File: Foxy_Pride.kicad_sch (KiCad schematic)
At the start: 30 parts, among them U1 TLC555CDR, U2 74HC4017D

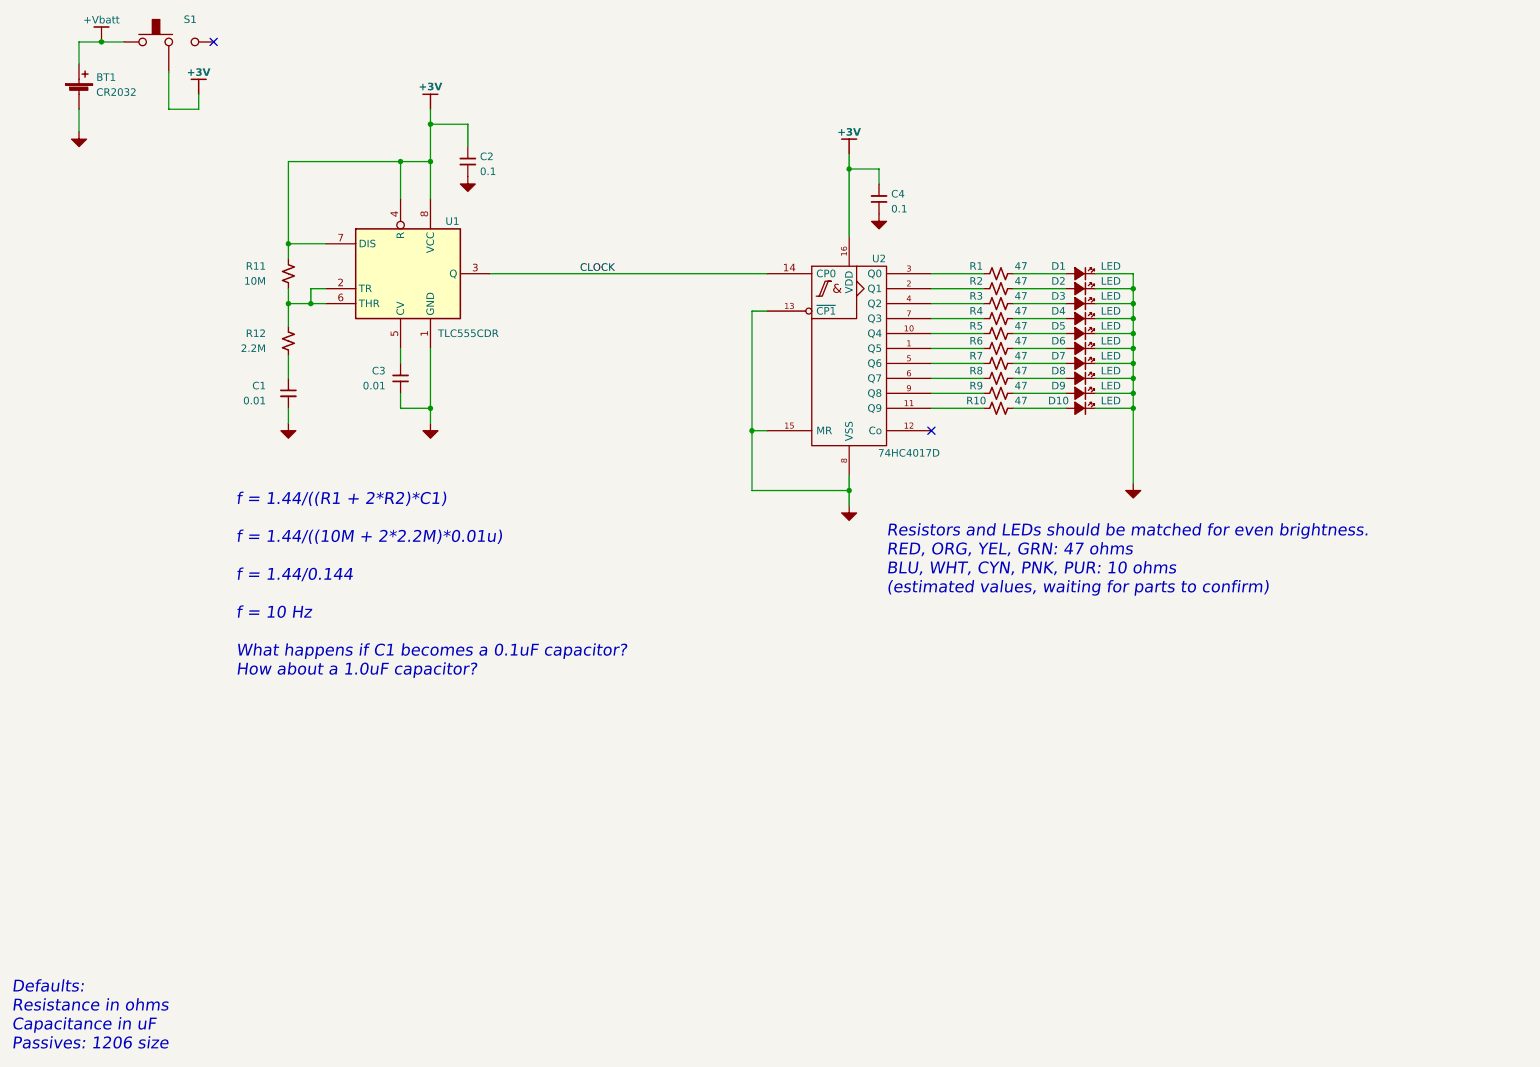
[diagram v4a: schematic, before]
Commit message: Changed schematic layout. Put resistor in correct spot. Update PCB.
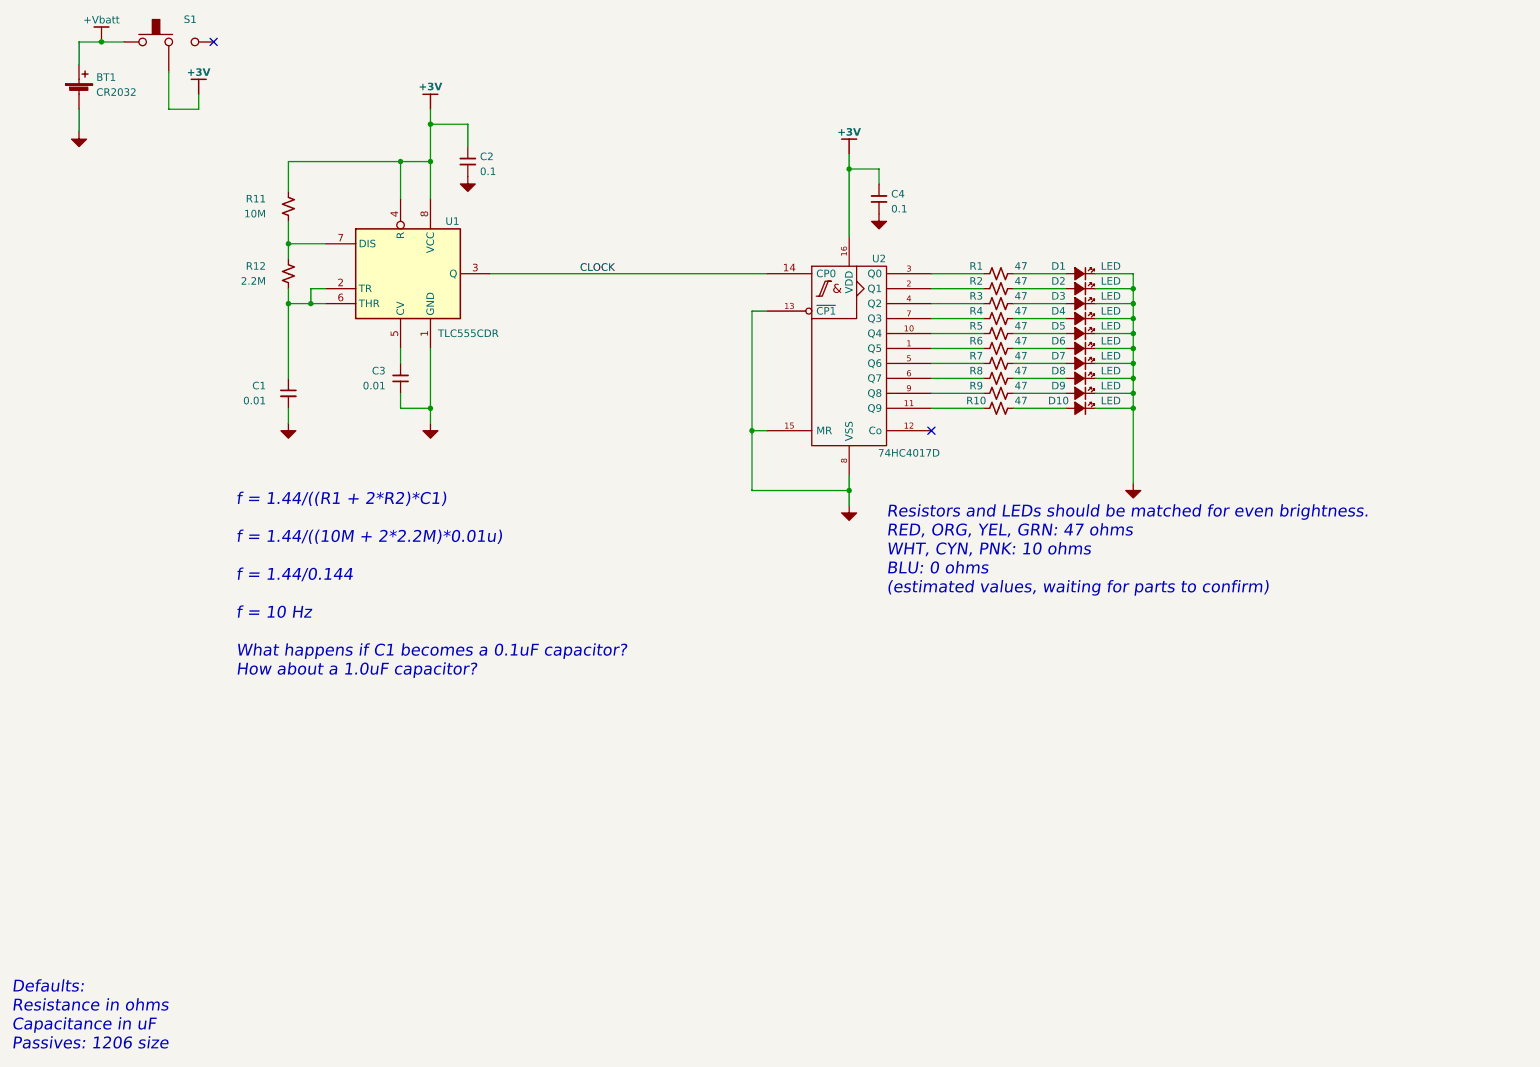
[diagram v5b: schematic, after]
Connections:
- net +3V: no longer U1.7 (DIS)
- net at R11.2, R12.1: now also U1.7 (DIS); no longer U1.2 (TR), U1.6 (THR)
- net at C1.1, R12.2: now also U1.2 (TR), U1.6 (THR)
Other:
- note added: "Resistors and LEDs should be matched for even brightness. RED, ORG, YEL, GRN: 47 ohms WHT, CYN, PNK: 10 ohms BLU: 0 ohms (estimated values, waiting for parts to confirm)"
- note removed: "Resistors and LEDs should be matched for even brightness. RED, ORG, YEL, GRN: 47 ohms BLU, WHT, CYN, PNK, PUR: 10 ohms (estimated values, waiting for parts to confirm)"
- moved on the sheet: R11, R12
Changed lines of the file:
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@@
-    (stroke (width 0) (type default) (color 0 0 0 0))
-  )
-  (wire (pts (xy 62.23 73.66) (xy 62.23 77.47))
-    (stroke (width 0) (type default) (color 0 0 0 0))
-  )
-  (wire (pts (xy 62.23 82.55) (xy 62.23 86.36))
     (stroke (width 0) (type default) (color 0 0 0 0))
   )
@@
     (stroke (width 0) (type default) (color 0 0 0 0))
   )
-  (wire (pts (xy 62.23 63.5) (xy 62.23 49.53))
+  (wire (pts (xy 62.23 54.61) (xy 62.23 49.53))
     (stroke (width 0) (type default) (color 0 0 0 0))
   )
@@
     (stroke (width 0) (type default) (color 0 0 0 0))
   )
+  (wire (pts (xy 62.23 73.66) (xy 62.23 86.36))
+    (stroke (width 0) (type default) (color 0 0 0 0))
+  )
   (wire (pts (xy 157.48 105.41) (xy 157.48 107.95))
     (stroke (width 0) (type default) (color 0 0 0 0))
@@
     (stroke (width 0) (type default) (color 0 0 0 0))
   )
-  (wire (pts (xy 62.23 66.04) (xy 62.23 63.5))
-    (stroke (width 0) (type default) (color 0 0 0 0))
-  )
   (wire (pts (xy 62.23 49.53) (xy 81.28 49.53))
     (stroke (width 0) (type default) (color 0 0 0 0))
@@
     (stroke (width 0) (type default) (color 0 0 0 0))
   )
+  (wire (pts (xy 62.23 71.12) (xy 62.23 73.66))
+    (stroke (width 0) (type default) (color 0 0 0 0))
+  )
   (wire (pts (xy 62.23 91.44) (xy 62.23 93.98))
     (stroke (width 0) (type default) (color 0 0 0 0))
@@
     (stroke (width 0) (type default) (color 0 0 0 0))
   )
+  (wire (pts (xy 62.23 59.69) (xy 62.23 63.5))
+    (stroke (width 0) (type default) (color 0 0 0 0))
+  )
   (wire (pts (xy 180.34 86.36) (xy 171.45 86.36))
     (stroke (width 0) (type default) (color 0 0 0 0))
@@
     (stroke (width 0) (type default) (color 0 0 0 0))
   )
-  (wire (pts (xy 62.23 71.12) (xy 62.23 73.66))
-    (stroke (width 0) (type default) (color 0 0 0 0))
-  )
   (wire (pts (xy 92.71 43.18) (xy 86.36 43.18))
     (stroke (width 0) (type default) (color 0 0 0 0))
@@
   )
   (wire (pts (xy 180.34 83.82) (xy 171.45 83.82))
+    (stroke (width 0) (type default) (color 0 0 0 0))
+  )
+  (wire (pts (xy 62.23 63.5) (xy 62.23 66.04))
     (stroke (width 0) (type default) (color 0 0 0 0))
   )
@@
     (effects (font (size 2 2) italic) (justify left bottom))
   )
-  (text "Resistors and LEDs should be matched for even brightness.\nRED, ORG, YEL, GRN: 47 ohms\nBLU, WHT, CYN, PNK, PUR: 10 ohms\n(estimated values, waiting for parts to confirm)"
+  (text "Resistors and LEDs should be matched for even brightness.\nRED, ORG, YEL, GRN: 47 ohms\nWHT, CYN, PNK: 10 ohms\nBLU: 0 ohms\n(estimated values, waiting for parts to confirm)"
     (at 163.83 123.19 0)
     (effects (font (size 2 2) italic) (justify left bottom))
@@
     (pin "2")
   )
-  (symbol (lib_id "Alpenglow:RES") (at 62.23 68.58 0) (unit 1)
-    (in_bom yes) (on_board yes)
-    (property "Reference" "R11" (id 0) (at 58.42 67.31 0)
-      (effects (font (size 1.27 1.27)) (justify right))
-    )
-    (property "Value" "10M" (id 1) (at 58.42 69.85 0)
-      (effects (font (size 1.27 1.27)) (justify right))
-    )
-    (property "Footprint" "Resistor_SMD:R_1206_3216Metric_Pad1.30x1.75mm_HandSolder" (id 2) (at 62.23 68.58 0)
-      (effects (font (size 1.27 1.27)) hide)
-    )
-    (property "Datasheet" "~" (id 3) (at 62.23 68.58 0)
+  (symbol (lib_id "Alpenglow:RES") (at 62.23 57.15 0) (unit 1)
+    (in_bom yes) (on_board yes)
+    (property "Reference" "R11" (id 0) (at 58.42 55.88 0)
+      (effects (font (size 1.27 1.27)) (justify right))
+    )
+    (property "Value" "10M" (id 1) (at 58.42 58.42 0)
+      (effects (font (size 1.27 1.27)) (justify right))
+    )
+    (property "Footprint" "Resistor_SMD:R_1206_3216Metric_Pad1.30x1.75mm_HandSolder" (id 2) (at 62.23 57.15 0)
+      (effects (font (size 1.27 1.27)) hide)
+    )
+    (property "Datasheet" "~" (id 3) (at 62.23 57.15 0)
       (effects (font (size 1.27 1.27)) hide)
     )
@@
     (pin "2")
   )
-  (symbol (lib_id "Alpenglow:RES") (at 62.23 80.01 0) (unit 1)
-    (in_bom yes) (on_board yes)
-    (property "Reference" "R12" (id 0) (at 58.42 78.74 0)
-      (effects (font (size 1.27 1.27)) (justify right))
-    )
-    (property "Value" "2.2M" (id 1) (at 58.42 81.28 0)
-      (effects (font (size 1.27 1.27)) (justify right))
-    )
-    (property "Footprint" "Resistor_SMD:R_1206_3216Metric_Pad1.30x1.75mm_HandSolder" (id 2) (at 62.23 80.01 0)
-      (effects (font (size 1.27 1.27)) hide)
-    )
-    (property "Datasheet" "~" (id 3) (at 62.23 80.01 0)
-      (effects (font (size 1.27 1.27)) hide)
-    )
+  (symbol (lib_id "Alpenglow:RES") (at 62.23 68.58 0) (unit 1)
+    (in_bom yes) (on_board yes)
+    (property "Reference" "R12" (id 0) (at 58.42 67.31 0)
+      (effects (font (size 1.27 1.27)) (justify right))
+    )
+    (property "Value" "2.2M" (id 1) (at 58.42 69.85 0)
+      (effects (font (size 1.27 1.27)) (justify right))
+    )
+    (property "Footprint" "Resistor_SMD:R_1206_3216Metric_Pad1.30x1.75mm_HandSolder" (id 2) (at 62.23 68.58 0)
+      (effects (font (size 1.27 1.27)) hide)
+    )
+    (property "Datasheet" "~" (id 3) (at 62.23 68.58 0)
+      (effects (font (size 1.27 1.27)) hide)
+    )

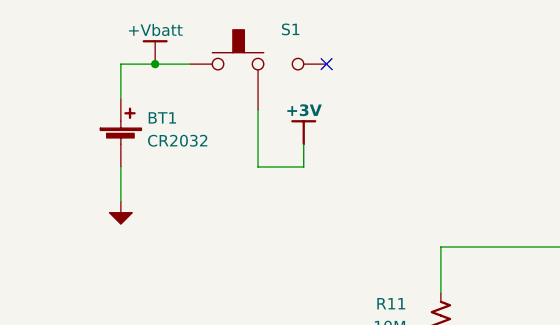
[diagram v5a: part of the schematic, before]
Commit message: Repositioned resistor and capacitor
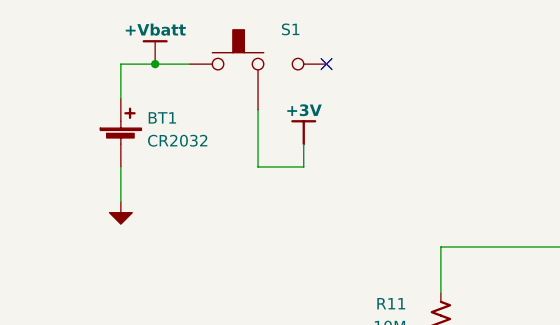
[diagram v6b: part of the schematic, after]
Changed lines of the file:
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@@
   (junction (at 157.48 105.41) (diameter 0) (color 0 0 0 0)
   )
+  (junction (at 30.48 29.21) (diameter 0) (color 0 0 0 0)
+  )
   (junction (at 140.97 95.25) (diameter 0) (color 0 0 0 0)
   )
@@
   )
   (junction (at 205.74 78.74) (diameter 0) (color 0 0 0 0)
-  )
-  (junction (at 30.48 29.21) (diameter 0) (color 0 0 0 0)
   )
   (junction (at 81.28 49.53) (diameter 0) (color 0 0 0 0)
@@
     (stroke (width 0) (type default) (color 0 0 0 0))
   )
+  (wire (pts (xy 30.48 29.21) (xy 34.29 29.21))
+    (stroke (width 0) (type default) (color 0 0 0 0))
+  )
   (wire (pts (xy 157.48 105.41) (xy 157.48 102.87))
     (stroke (width 0) (type default) (color 0 0 0 0))
@@
     (stroke (width 0) (type default) (color 0 0 0 0))
   )
-  (wire (pts (xy 30.48 29.21) (xy 26.67 29.21))
+  (wire (pts (xy 26.67 29.21) (xy 30.48 29.21))
     (stroke (width 0) (type default) (color 0 0 0 0))
   )
@@
   )
   (wire (pts (xy 81.28 49.53) (xy 86.36 49.53))
-    (stroke (width 0) (type default) (color 0 0 0 0))
-  )
-  (wire (pts (xy 34.29 29.21) (xy 30.48 29.21))
     (stroke (width 0) (type default) (color 0 0 0 0))
   )
@@
     (pin "1")
     (pin "2")
-  )
-  (symbol (lib_id "Alpenglow:+Vbatt") (at 25.4 29.21 0) (unit 1)
-    (in_bom yes) (on_board yes) (fields_autoplaced)
-    (property "Reference" "#PWR0101" (id 0) (at 25.4 33.02 0)
-      (effects (font (size 1.27 1.27)) hide)
-    )
-    (property "Value" "+Vbatt" (id 1) (at 30.48 25.4785 0))
-    (property "Footprint" "" (id 2) (at 25.4 29.21 0)
-      (effects (font (size 1.27 1.27)) hide)
-    )
-    (property "Datasheet" "" (id 3) (at 25.4 29.21 0)
-      (effects (font (size 1.27 1.27)) hide)
-    )
-    (pin "")
   )
   (symbol (lib_id "Device:Battery_Cell") (at 26.67 38.1 0) (unit 1)
@@
     (pin "9")
   )
+  (symbol (lib_name "+Vbatt_1") (lib_id "Alpenglow:+Vbatt") (at 30.48 29.21 0) (unit 1)
+    (in_bom yes) (on_board yes) (fields_autoplaced)
+    (property "Reference" "#PWR0101" (id 0) (at 30.48 33.02 0)
+      (effects (font (size 1.27 1.27)) hide)
+    )
+    (property "Value" "+Vbatt" (id 1) (at 30.48 25.4443 0)
+      (effects (font (size 1.27 1.27) bold))
+    )
+    (property "Footprint" "" (id 2) (at 30.48 29.21 0)
+      (effects (font (size 1.27 1.27)) hide)
+    )
+    (property "Datasheet" "" (id 3) (at 30.48 29.21 0)
+      (effects (font (size 1.27 1.27)) hide)
+    )
+    (pin "")
+  )
   (symbol (lib_id "Alpenglow:GND") (at 162.56 58.42 0) (unit 1)
     (in_bom yes) (on_board yes) (fields_autoplaced)
@@
       (reference "#PWR010") (unit 1) (value "GND") (footprint "")
     )
-    (path "/0f81970b-f55e-4039-a8ff-40c0a07bab88"
+    (path "/d1887814-20c5-4133-b31c-559149e546cd"
       (reference "#PWR0101") (unit 1) (value "+Vbatt") (footprint "")
     )

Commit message: Updated Final Design
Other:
- note added: "Resistors and LEDs should be matched for even brightness. WHT, CYN, PNK, RED, YEL, ORNG, GRN: 1k ohms BLU, PURP: 470 ohms (values based off of 2 CR2016 batteries)"
- note removed: "Resistors and LEDs should be matched for even brightness. RED, ORG, YEL, GRN: 47 ohms WHT, CYN, PNK: 10 ohms BLU: 0 ohms (estimated values, waiting for parts to confirm)"
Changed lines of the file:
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@@
     (effects (font (size 2 2) italic) (justify left bottom))
   )
-  (text "Resistors and LEDs should be matched for even brightness.\nRED, ORG, YEL, GRN: 47 ohms\nWHT, CYN, PNK: 10 ohms\nBLU: 0 ohms\n(estimated values, waiting for parts to confirm)"
+  (text "Resistors and LEDs should be matched for even brightness.\nWHT, CYN, PNK, RED, YEL, ORNG, GRN: 1k ohms\nBLU, PURP: 470 ohms\n(values based off of 2 CR2016 batteries)"
     (at 163.83 123.19 0)
     (effects (font (size 2 2) italic) (justify left bottom))
